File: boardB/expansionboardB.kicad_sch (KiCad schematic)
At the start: 48 parts, among them J1 USB_C_Receptacle, J3 HDMI_A, SW4 ESPPROG, U1 ESP32-S3-WROOM-1, U2 GPIO_U2, U4 GPIO_U4, U5 SII1136CTU, U7 MAX20022ATIA+T, t1V2 1V2_TEST, t3V3 3V3_TEST

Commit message: Board updates
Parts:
- added D1: LED, LED_SMD:LED_1206_3216Metric_Pad1.42x1.75mm_HandSolder, symbol Device:LED
- added R17: 33, Resistor_SMD:R_0603_1608Metric_Pad0.98x0.95mm_HandSolder, symbol Device:R
- added SW1: ESPRST, Button_Switch_SMD:SW_Tactile_SPST_NO_Straight_CK_PTS636Sx25SMTRLFS, symbol Switch:SW_Push
- added t5V1: 5V_IN_TEST, TestPoint:TestPoint_Pad_D1.5mm, symbol Connector:TestPoint
- added tDIAG1: DIAGNOSIS, TestPoint:TestPoint_Pad_D1.5mm, symbol Connector:TestPoint
- added tPG1: PG1_TEST, TestPoint:TestPoint_Pad_D1.5mm, symbol Connector:TestPoint
- added tPG2: PG2_TEST, TestPoint:TestPoint_Pad_D1.5mm, symbol Connector:TestPoint
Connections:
- net 5V: now also t5V1.1
- net ESP_RST: now also SW1.2
- net GND: now also D1.1 (K), SW1.1
- net PG_1: now also tPG1.1
- net LEDPWR: now reaches U2.36 (Pin_36)
- net LEDPWR: now also R17.1
- net at U4.8 (Pin_8): now also tDIAG1.1
- net at U7.10 (PG2): now also tPG2.1
- new net: D1.2 (A), R17.2
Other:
- moved on the sheet: C4, C5, JTAG1, SW4

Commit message: board update
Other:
- note added: "OR 11.5K"
- note added: "OR 1K"
- note added: "OR 5K"
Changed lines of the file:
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@@
+		)
+	)
+	(text "OR 1K"
+		(exclude_from_sim no)
+		(at 243.078 234.95 0)
+		(effects
+			(font
+				(size 0.762 0.762)
+			)
+			(justify left)
 		)
 	)
@@
 		)
 	)
+	(text "OR 5K"
+		(exclude_from_sim no)
+		(at 247.904 251.46 0)
+		(effects
+			(font
+				(size 0.762 0.762)
+			)
+			(justify left)
+		)
+	)
 	(text "Micro SD Card"
 		(exclude_from_sim no)
@@
 		)
 	)
+	(text "OR 5K"
+		(exclude_from_sim no)
+		(at 275.59 255.524 0)
+		(effects
+			(font
+				(size 0.762 0.762)
+			)
+			(justify left)
+		)
+	)
 	(text "A/V HDMI output"
 		(exclude_from_sim no)
@@
 		)
 	)
+	(text "OR 11.5K"
+		(exclude_from_sim no)
+		(at 264.414 236.982 0)
+		(effects
+			(font
+				(size 0.762 0.762)
+			)
+			(justify left)
+		)
+	)

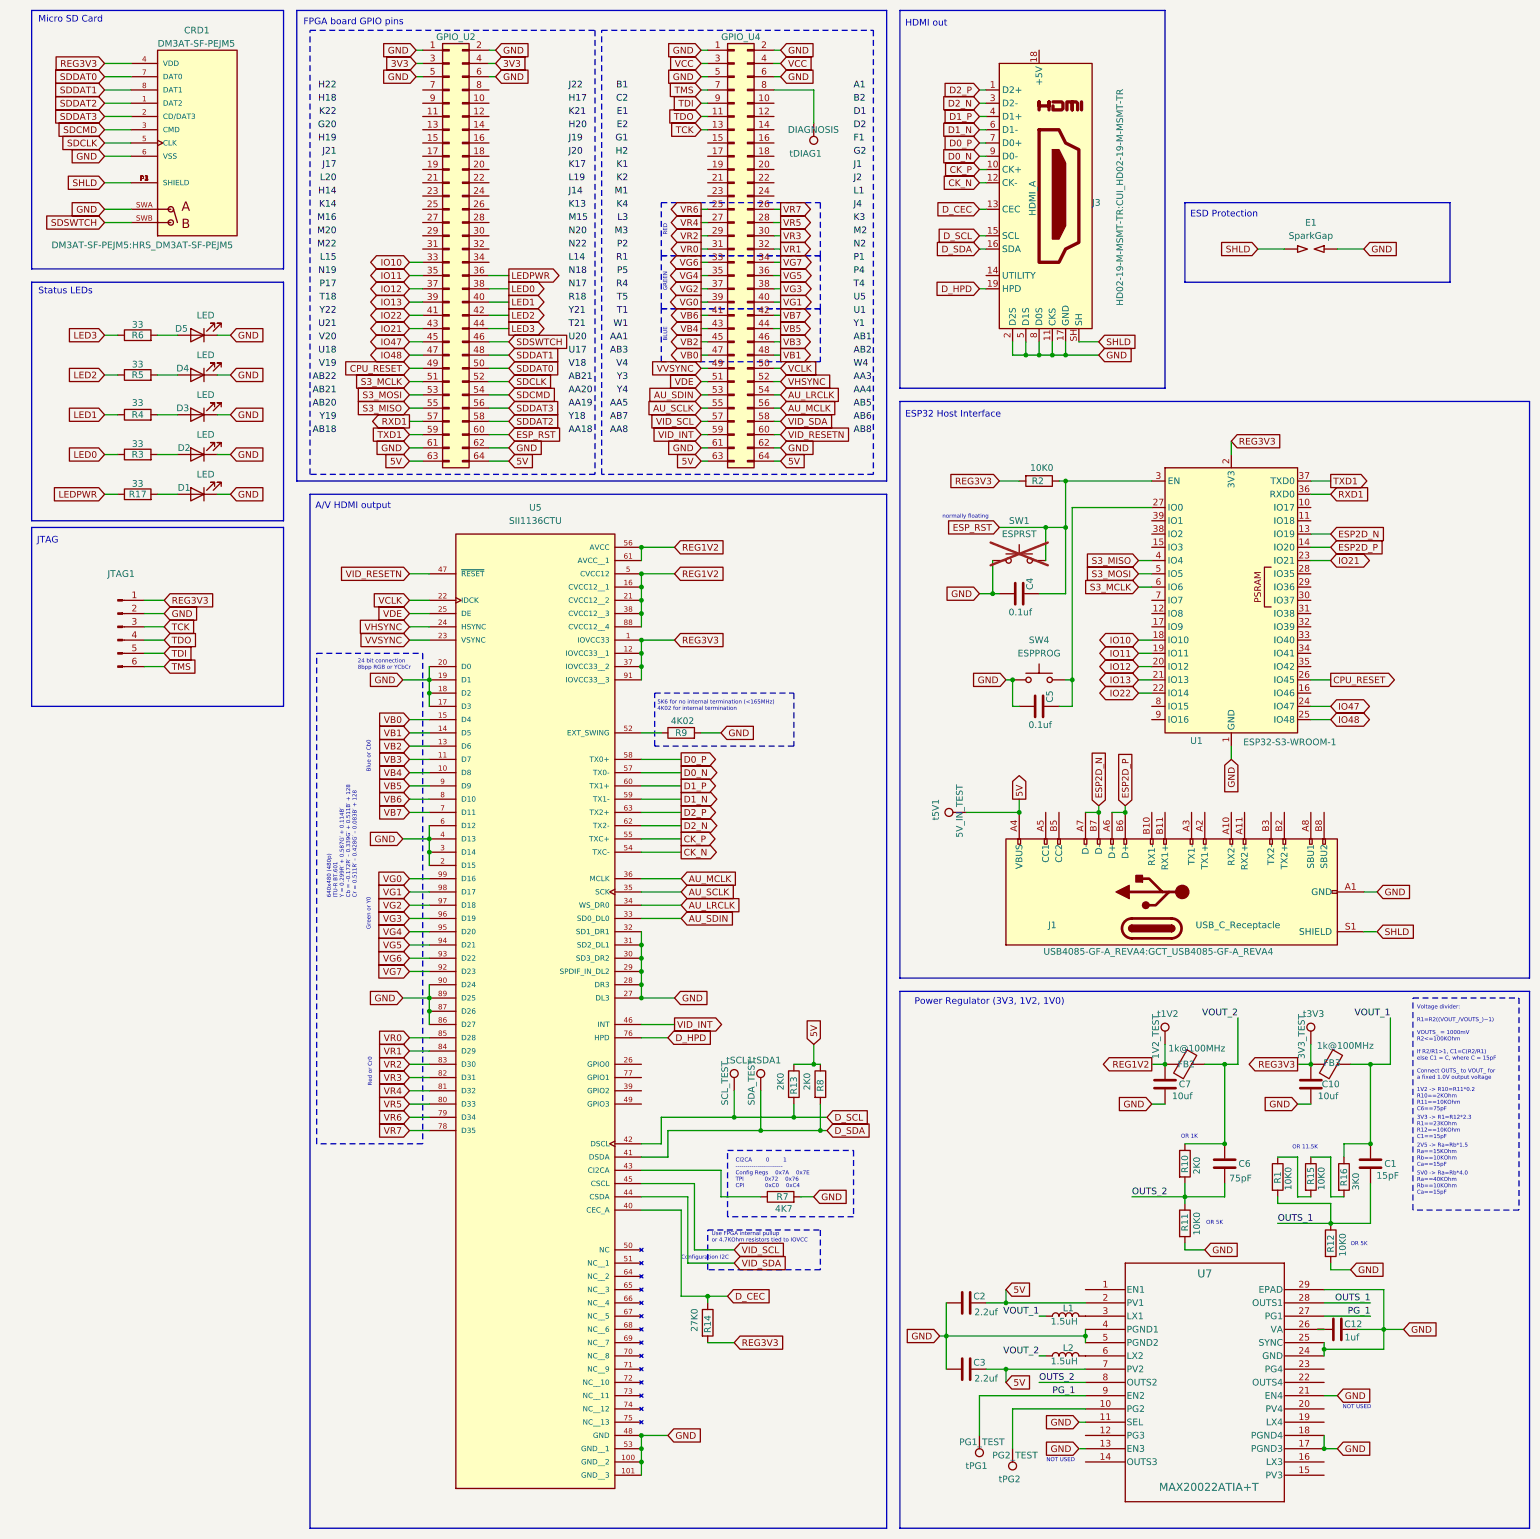
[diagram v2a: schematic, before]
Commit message: Started to get rid of the video and audio chips and circuitry
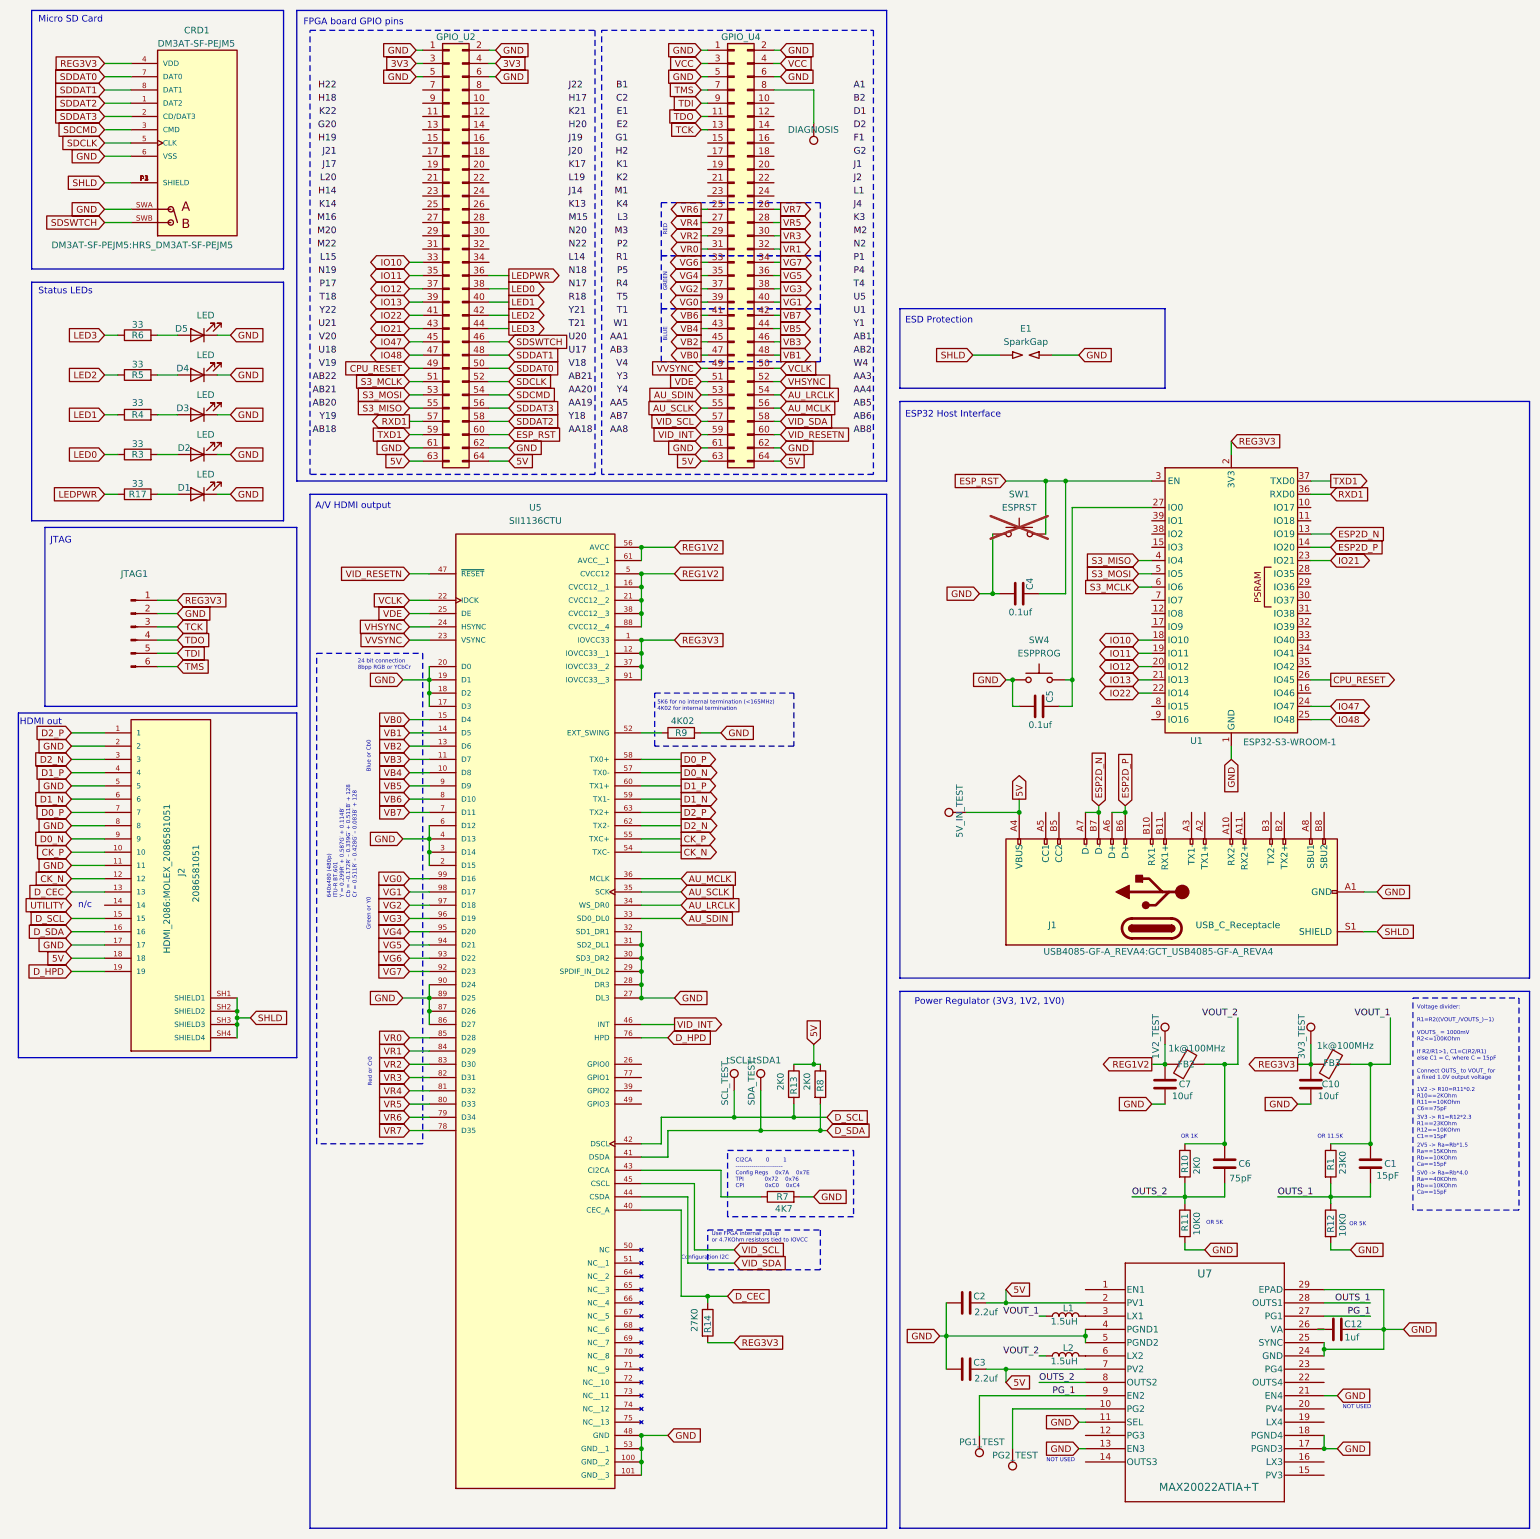
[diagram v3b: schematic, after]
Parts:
- removed J3: HDMI_A, HD02-19-M-MSMT-TR:CUI_HD02-19-M-MSMT-TR, symbol Connector:HDMI_A
- removed R15, R2: 10K0, Resistor_SMD:R_0603_1608Metric_Pad0.98x0.95mm_HandSolder, symbol Device:R
- removed R16: 3K0, Resistor_SMD:R_0603_1608Metric_Pad0.98x0.95mm_HandSolder, symbol Device:R
- added J2: 2086581051, HDMI_2086:MOLEX_2086581051, symbol HDMI_2086:2086581051
- R1: value 10K0 -> 23K0
- t1V2, t3V3, t5V1, tDIAG1, tPG1, tPG2, tSCL1, tSDA1: footprint TestPoint:TestPoint_Pad_D1.5mm -> TestPoint:TestPoint_Pad_1.0x1.0mm
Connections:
- net 5V: now also J2.18
- net CK_N: now also J2.12
- net CK_P: now also J2.10
- net D0_N: now also J2.9
- net D0_P: now also J2.7
- net D1_N: now also J2.6
- net D1_P: now also J2.4
- net D2_N: now also J2.3
- net D2_P: now also J2.1
- net D_CEC: now also J2.13
- net D_HPD: now also J2.19
- net D_SCL: now also J2.15
- net D_SDA: now also J2.16
- net GND: now also J2.11, J2.17, J2.2, J2.5, J2.8
- net SHLD: now also J2.SH1 (SHIELD1), J2.SH2 (SHIELD2), J2.SH3 (SHIELD3), J2.SH4 (SHIELD4)
- net VOUT_1: now also R1.1
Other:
- note added: "n/c"
- note removed: "normally floating"
- moved on the sheet: E1, JTAG1, R1, R12, SW1

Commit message: Updates to board and mechanical files Rebuilt tinyremote exe Updated device with WNS fixes
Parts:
- R1: value 23K0 -> 11K5
- R12: value 10K0 -> 5K0
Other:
- note removed: "OR 11.5K"

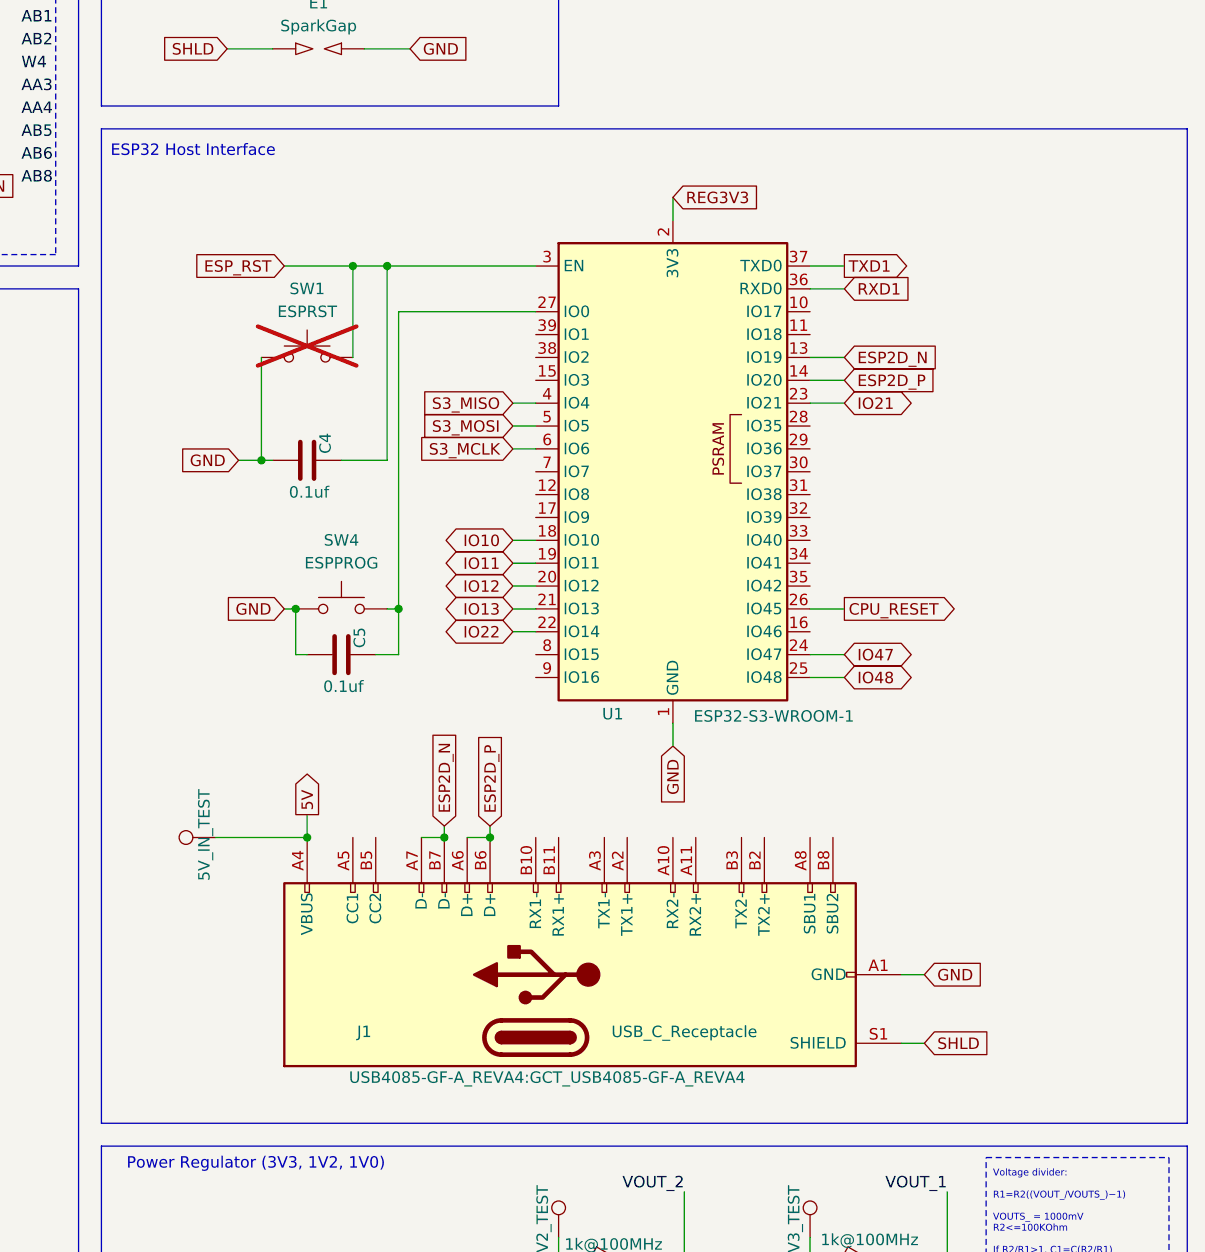
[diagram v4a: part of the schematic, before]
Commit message: Board B reshaped
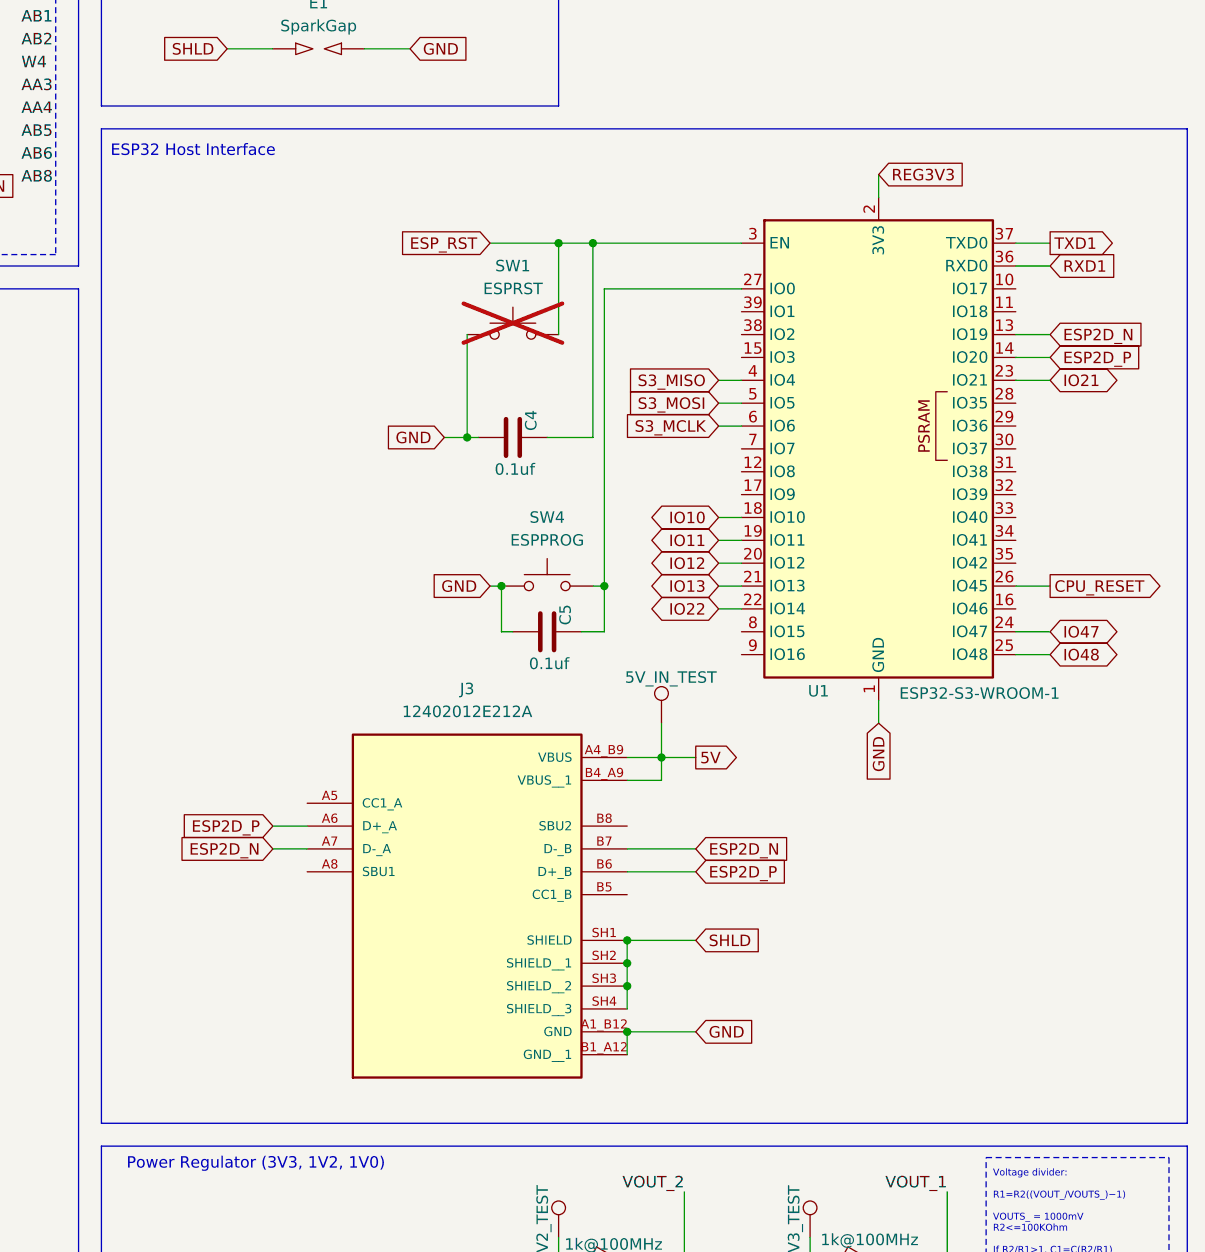
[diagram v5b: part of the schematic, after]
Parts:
- removed J1: USB_C_Receptacle, USB4085-GF-A_REVA4:GCT_USB4085-GF-A_REVA4, symbol Connector:USB_C_Receptacle
- removed t5V1: 5V_IN_TEST, TestPoint:TestPoint_Pad_1.0x1.0mm, symbol Connector:TestPoint
- added J3: 12402012E212A, 12402012E212A:AMPHENOL_12402012E212A, symbol 12402012E212A:12402012E212A
- added t5V2: 5V_IN_TEST, TestPoint:TestPoint_Pad_1.0x1.0mm, symbol Connector:TestPoint
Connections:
- net 5V: now also J3.A4_B9 (VBUS), J3.B4_A9 (VBUS__1), t5V2.1
- net ESP2D_N: now also J3.A7 (D-_A), J3.B7 (D-_B)
- net ESP2D_P: now also J3.A6 (D+_A), J3.B6 (D+_B)
- net GND: now also J3.A1_B12 (GND), J3.B1_A12 (GND__1)
- net SHLD: now also J3.SH1 (SHIELD), J3.SH2 (SHIELD__1), J3.SH3 (SHIELD__2), J3.SH4 (SHIELD__3)
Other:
- moved on the sheet: C4, C5, SW1, SW4, U1
